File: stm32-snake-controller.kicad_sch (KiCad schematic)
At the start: 45 parts, among them J101 Barrel_Jack_MountingPin, J101 Tag Connector, J103 JST 2.54 Header, Q101 AO3501A, SW106 SW_Push, U101 STM32F401RCTx, U102 USBLC6-2SC6, U104 M24C64-RMN, Y101 16MHz, Y103 32.768kHz

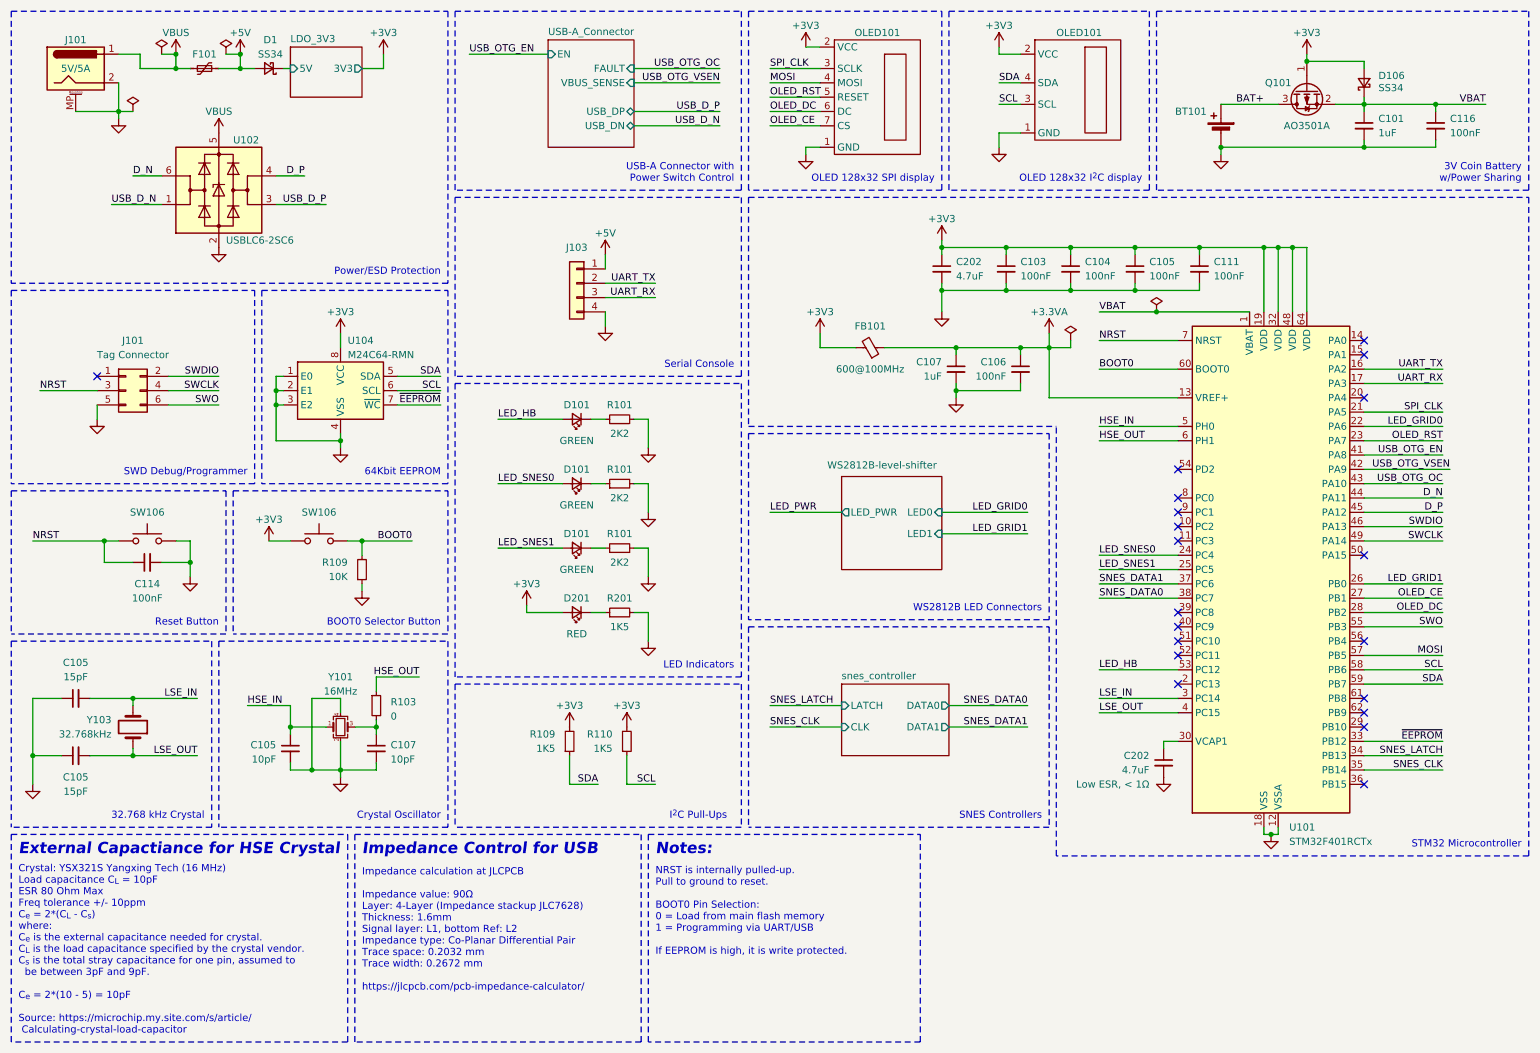
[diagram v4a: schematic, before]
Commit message: add mounting holes and reassign pins
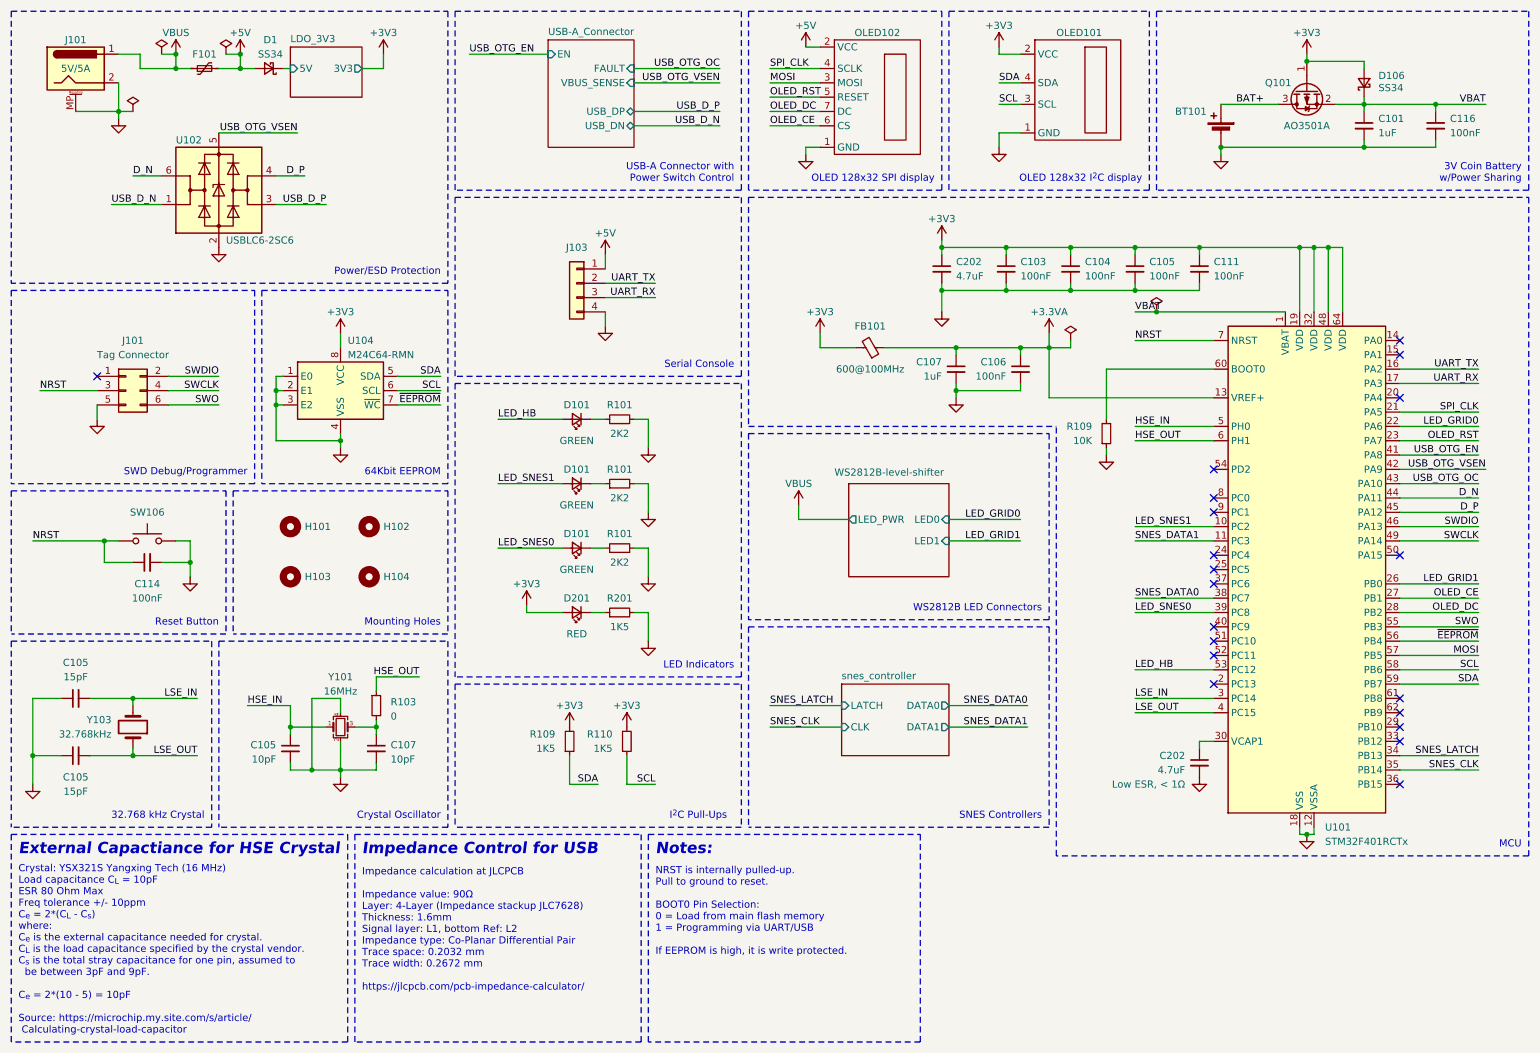
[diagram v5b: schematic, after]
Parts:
- removed SW106: SW_Push, User_Footprint:XKB-Connectivity-TS-1187A-B-A-B, symbol Switch:SW_Push
- added H101, H102, H103, H104: MountingHole, MountingHole:MountingHole_3.2mm_M3, symbol Mechanical:MountingHole
- OLED101: footprint Connector_JST:JST_XH_B4B-XH-A_1x04_P2.50mm_Vertical -> Connector_JST:JST_PH_B4B-PH-K_1x04_P2.00mm_Vertical
- OLED102: renamed from OLED101; footprint Connector_JST:JST_XH_B7B-XH-A_1x07_P2.50mm_Vertical -> Connector_JST:JST_PH_B7B-PH-K_1x07_P2.00mm_Vertical; now left out of the parts list
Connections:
- net +3V3: no longer OLED102.2 (VCC)
- net +5V: now also OLED102.2 (VCC)
- net LED_SNES0: now also D101.2 (A), U101.39 (PC8); no longer D101.2 (A), U101.24 (PC4)
- net LED_SNES1: now also D101.2 (A), U101.10 (PC2); no longer D101.2 (A), U101.25 (PC5)
- net MOSI: now also OLED102.3 (MOSI); no longer OLED102.4 (MOSI)
- net OLED_CE: now also OLED102.6 (CS); no longer OLED102.7 (CS)
- net OLED_DC: now also OLED102.7 (DC); no longer OLED102.6 (DC)
- net SNES_DATA1: now also U101.11 (PC3); no longer U101.37 (PC6)
- net SPI_CLK: now also OLED102.4 (SCLK); no longer OLED102.3 (SCLK)
- net USB_OTG_VSEN: now also U102.5 (VBUS)
- net VBUS: no longer U102.5 (VBUS)
- net ~{EEPROM}: now also U101.56 (PB4); no longer U101.33 (PB12)
- net BOOT0: no longer names the net of R109.2, U101.60 (BOOT0)
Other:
- note added: "MCU"
- note added: "Mounting Holes"
- note removed: "BOOT0 Selector Button"
- note removed: "STM32 Microcontroller"
- moved on the sheet: C202, U101

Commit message: update BOM
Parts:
- H101, H102, H103, H104, J101: now left out of the parts list
- U101: value STM32F401RCTx -> STM32F446RCTx; LCSC C74524 -> C915971
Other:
- note added: "180 MHz 256K Flash 128K RAM"
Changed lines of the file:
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@@
     (effects (font (size 1.27 1.27)) (justify left bottom))
   )
+  (text "180 MHz\n256K Flash\n128K RAM" (at 238.76 113.03 0)
+    (effects (font (size 1.27 1.27)) (justify left bottom))
+  )
   (text "Serial Console" (at 142.24 77.47 0)
     (effects (font (size 1.27 1.27)) (justify right bottom))
@@
   )
   (symbol (lib_id "Mechanical:MountingHole") (at 63.5 105.41 0) (unit 1)
-    (in_bom yes) (on_board yes) (dnp no) (fields_autoplaced)
+    (in_bom no) (on_board yes) (dnp no) (fields_autoplaced)
     (property "Reference" "H101" (at 66.04 105.41 0)
       (effects (font (size 1.27 1.27)) (justify left))
@@
       (effects (font (size 1.27 1.27)) hide)
     )
+    (property "LCSC" "" (at 63.5 105.41 0)
+      (effects (font (size 1.27 1.27)) hide)
+    )
+    (property "Mouser" "" (at 63.5 105.41 0)
+      (effects (font (size 1.27 1.27)) hide)
+    )
     (instances
       (project "stm32-snake-controller"
@@
       (effects (font (size 1.27 1.27)) (justify left))
     )
-    (property "Value" "STM32F401RCTx" (at 247.0659 161.29 0)
+    (property "Value" "STM32F446RCTx" (at 247.0659 161.29 0)
       (effects (font (size 1.27 1.27)) (justify left))
     )
@@
       (effects (font (size 1.27 1.27)) hide)
     )
-    (property "LCSC" "C74524" (at 242.57 113.03 0)
+    (property "LCSC" "C915971" (at 242.57 113.03 0)
       (effects (font (size 1.27 1.27)) hide)
     )
@@
   )
   (symbol (lib_id "Mechanical:MountingHole") (at 77.47 114.3 0) (unit 1)
-    (in_bom yes) (on_board yes) (dnp no) (fields_autoplaced)
+    (in_bom no) (on_board yes) (dnp no) (fields_autoplaced)
     (property "Reference" "H104" (at 80.01 114.3 0)
       (effects (font (size 1.27 1.27)) (justify left))
@@
       (effects (font (size 1.27 1.27)) hide)
     )
+    (property "LCSC" "" (at 77.47 114.3 0)
+      (effects (font (size 1.27 1.27)) hide)
+    )
+    (property "Mouser" "" (at 77.47 114.3 0)
+      (effects (font (size 1.27 1.27)) hide)
+    )
     (instances
       (project "stm32-snake-controller"
@@
   )
   (symbol (lib_id "Connector:Barrel_Jack_MountingPin") (at 25.4 24.13 0) (unit 1)
-    (in_bom yes) (on_board yes) (dnp no)
+    (in_bom no) (on_board yes) (dnp no)
     (property "Reference" "J101" (at 25.4 19.05 0)
       (effects (font (size 1.27 1.27)))
@@
   )
   (symbol (lib_id "Mechanical:MountingHole") (at 63.5 114.3 0) (unit 1)
-    (in_bom yes) (on_board yes) (dnp no) (fields_autoplaced)
+    (in_bom no) (on_board yes) (dnp no) (fields_autoplaced)
     (property "Reference" "H103" (at 66.04 114.3 0)
       (effects (font (size 1.27 1.27)) (justify left))
@@
       (effects (font (size 1.27 1.27)) hide)
     )
+    (property "LCSC" "" (at 63.5 114.3 0)
+      (effects (font (size 1.27 1.27)) hide)
+    )
+    (property "Mouser" "" (at 63.5 114.3 0)
+      (effects (font (size 1.27 1.27)) hide)
+    )
     (instances
       (project "stm32-snake-controller"
@@
   )
   (symbol (lib_id "Mechanical:MountingHole") (at 77.47 105.41 0) (unit 1)
-    (in_bom yes) (on_board yes) (dnp no) (fields_autoplaced)
+    (in_bom no) (on_board yes) (dnp no) (fields_autoplaced)
     (property "Reference" "H102" (at 80.01 105.41 0)
       (effects (font (size 1.27 1.27)) (justify left))
@@
       (effects (font (size 1.27 1.27)) hide)
     )
+    (property "LCSC" "" (at 77.47 105.41 0)
+      (effects (font (size 1.27 1.27)) hide)
+    )
+    (property "Mouser" "" (at 77.47 105.41 0)
+      (effects (font (size 1.27 1.27)) hide)
+    )
